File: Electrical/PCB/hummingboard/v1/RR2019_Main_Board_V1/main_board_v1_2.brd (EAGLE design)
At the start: 100 x 75 mm, 138 parts, among them CN1 MIRCO_B, IC1 OR_SC70-5, J10 I2C_5V_4, J11 SERVO_LEFT, J12 SERVO_RIGHT, J13 ESC, J14 5V_INPUT, J15 QUAD_ENCODER_2, J16 7.2V_INPUT, J17 I2C_5V_FXIO_1, J18 I2C_5V_FXIO_2, J19 JETSON_TRIGGER, J2 REAR_ENCODER, J20 QUAD_ENCODER_1, J21 BLDC_HALL, J22 SPI_FXIO_1, J3 FRONT_ENCODER, J4 I2C_3V3_1, J5 SPI_2, J6 WIRELESS_MODULE, J7 UART_0, J8 UART_2, J9 STEERING_ANGLE, Q1 BSS138, Q2 BSS138, Q3 DMP2066LSN, Q4 BSS138, Q5 BSS138, Q6 BSS138, Q7 BSS138, Q8 BSS138, U1 MPU-9250(IMU)

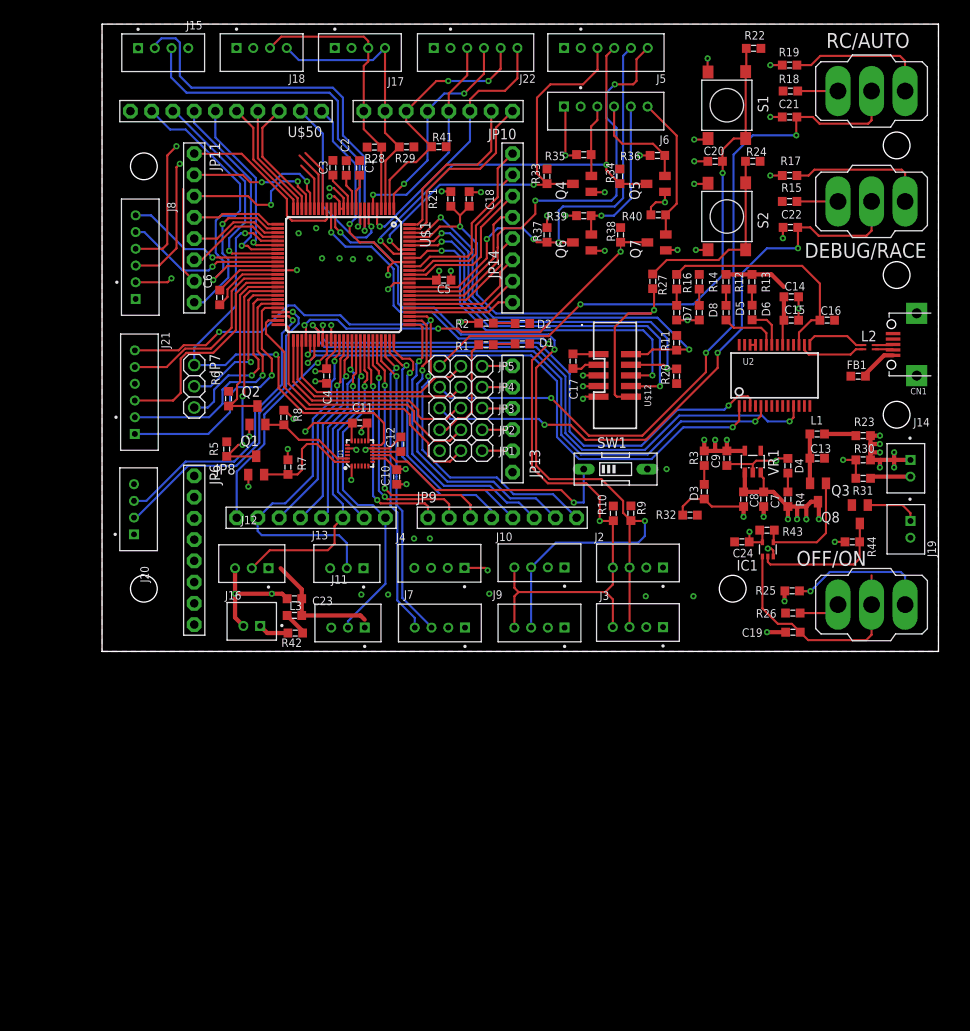
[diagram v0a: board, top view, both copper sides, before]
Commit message: add 1.8V LDO and IMU change to ICM-20948
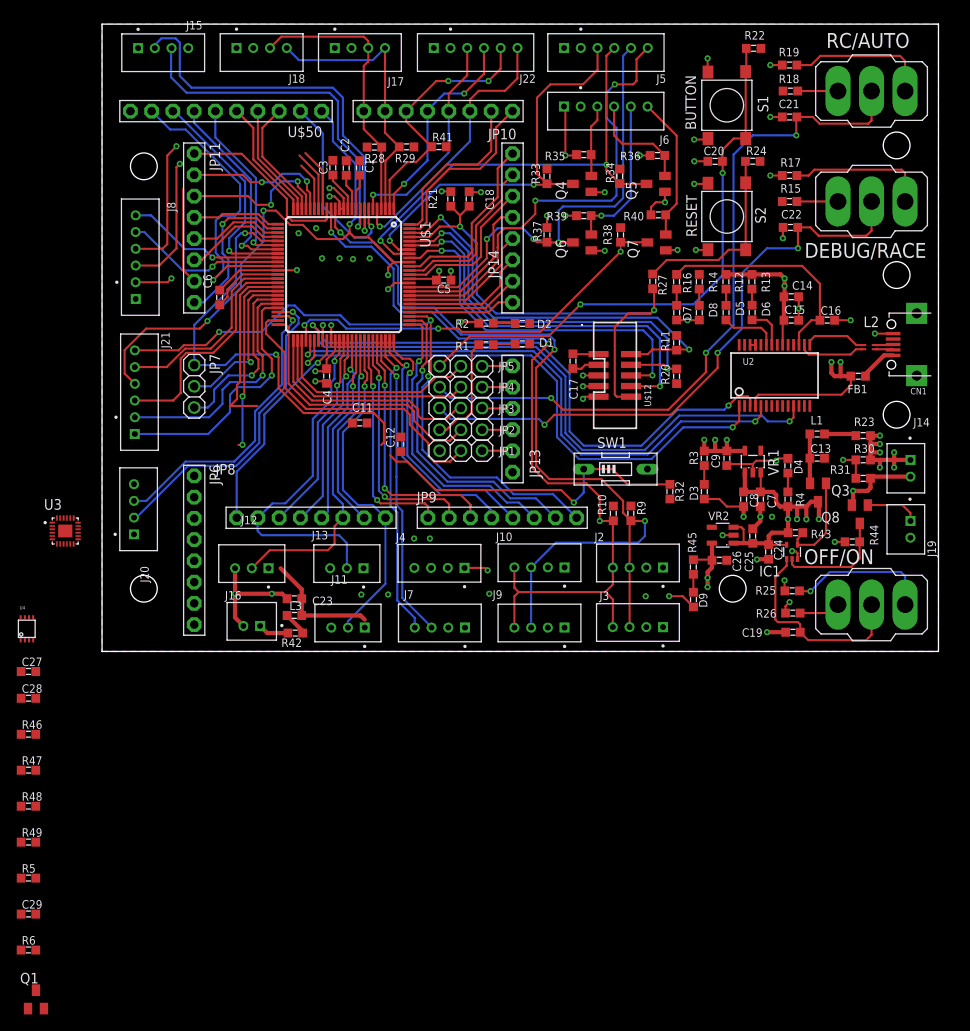
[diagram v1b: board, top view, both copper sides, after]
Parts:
- removed C10: 10nF, RobotRacing2019_Master:0603SMT
- removed Q2: BSS138, RobotRacing2019_Master:SOT23
- removed R7, R8: 10k, RobotRacing2019_Master:0603SMT
- removed U1: MPU-9250(IMU), RobotRacing2019_Master:QFN24-3X3
- added C25, C26: 1uF, RobotRacing2019_Master:0603SMT
- added C27, C28: 0.1u, RobotRacing2019_Master:0603SMT
- added C29: 0.1uF, RobotRacing2019_Master:0603SMT
- added D9: LED_GREEN, RobotRacing2019_Master:0603SMT
- added R45: 150, RobotRacing2019_Master:0603SMT
- added R46, R47, R48, R49: 1k, RobotRacing2019_Master:0603SMT
- added U3: ICM-20948, RobotRacing2019_Master:QFN40P300X300X105-25N
- added U4: PCA9306, RobotRacing2019_Master:PSOP-8
- added VR2: ADP121-AUJZ18, RobotRacing2019_Master:TSOT23-5
- D3, D4: value LED0603 -> LED_GREEN
- R3, R4: value (none) -> 150
- R5: value 10k -> 200k
- moved R6 70.1 mm to (-8.80, -35.7), turned to 0 degrees
- moved Q1 69.1 mm to (-7.90, -41.6)
- moved R5 56.5 mm to (-8.80, -27.1), turned to 0 degrees
- moved R32 3.69 mm to (67.9, 19.1), turned to 90 degrees
- moved C24 3.42 mm to (79.7, 11.9), turned to 90 degrees
- moved R43 3.41 mm to (82.9, 14.2)
- moved IC1 2.92 mm to (82.5, 11.9)
- moved C7 0.40 mm to (78.7, 18.2)
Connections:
- new net +1.8V: C11.2, C26.1, C27.2, C29.2, R45.2, R46.2, R47.2, R6.2, SW1.2, U3.13, U3.22, U3.8, U4.1, VR2.5
- new net I2C1_1.8_SCL: R46.1, U3.23, U4.2
- new net I2C_1.8_SDA: R47.1, U3.24, U4.3
- new net N$16: C28.2, R5.1, U4.7, U4.8
- new net N$37: Q1.1, U3.12
- new net N$42: D9.1, R45.1
- net +3V3: no longer C10.2, C11.2, Q1.1, Q2.1, R7.2, R8.2, SW1.2, U1.1, U1.13, U1.8
- net +VDD: now also C25.1, R48.2, R49.2, VR2.1, VR2.3; no longer R6.2
- net 3V3_SCL_1: no longer Q2.2, R8.1, U1.23
- net 3V3_SDA_1: no longer Q1.2, R7.1, U1.24
- net ADC0_SE10_/_ACMP0_IN5: now also Q1.3, R6.1; no longer U1.12
- net ADC0_SE14_/_PTC16: now also U3.11
- net GND: now also C25.2, C26.2, C27.1, C28.1, C29.1, D9.2, Q1.2, U3.18, U3.20, U3.25, U4.4, VR2.2; no longer C10.1, U1.11, U1.18, U1.20
- net I2C1_SDA: now also R49.1, U4.5; no longer Q1.3, R5.1
- net I2C1__SCL: now also R48.1, U4.6; no longer Q2.3, R6.1
- net N$10: now also U3.10; no longer U1.10
- net N$22: now also U3.9; no longer U1.9
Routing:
- net +1.8V: track 0.00 -> 129.0 mm, vias 0 -> 2
- net +VUSB: track 13.4 -> 64.7 mm, vias 0 -> 4
- net PTA11_/_FTM1_CH5: track 26.9 -> 70.8 mm, vias 2 -> 4
- net +3V3: track 45.9 -> 30.3 mm, vias 19 -> 11
- net 3V3_SDA_1: track 13.8 -> 0.00 mm
- net +VDD: track 65.3 -> 78.0 mm, vias 10 -> 11
- net 3V3_SCL_1: track 11.5 -> 0.00 mm
- net N$22: track 31.6 -> 39.9 mm
- net I2C1_SDA: track 28.1 -> 22.6 mm
- net POWER_SHUT_DOWN: track 28.2 -> 24.7 mm
- net N$10: track 3.40 -> 0.00 mm
- net N$39: track 14.3 -> 11.2 mm
- net N$38: track 16.2 -> 13.5 mm
- net N$31: track 88.4 -> 85.8 mm
- net N$42: track 0.00 -> 2.15 mm
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
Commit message: signal connection complete
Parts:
- moved Q1 75.6 mm to (22.2, 27.7)
- moved R6 72.1 mm to (19.2, 30.7), turned to 180 degrees
- moved C29 71.9 mm to (32.5, 27.4), turned to 180 degrees
- moved R47 56.7 mm to (33.9, 23.1), turned to 90 degrees
- moved R49 55.5 mm to (21.1, 23.9)
- moved R5 53.3 mm to (18.7, 18.5), turned to 180 degrees
- moved R48 48.2 mm to (18.7, 21.1), turned to 180 degrees
- moved R46 46.7 mm to (27.6, 19.3), turned to 270 degrees
- moved C27 40.6 mm to (25.5, 19.3), turned to 90 degrees
- moved C28 39.3 mm to (22.3, 18.5), turned to 180 degrees
- moved U4 36.5 mm to (22.5, 21.2), turned to 90 degrees
- moved U3 36.1 mm to (30.5, 23.8), turned to 180 degrees
- moved U$38 12.7 mm to (78.2, 3.20)
- moved C12 7.32 mm to (28.9, 27.5), turned to 180 degrees
- moved C11 5.10 mm to (27.0, 23.9), turned to 90 degrees
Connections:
- removed net 3V3_SCL_1: J4.3
- removed net 3V3_SDA_1: J4.4
- removed net I2C_1.8_SDA: R47.1, U3.24, U4.3
- new net I2C1_1.8_SDA: J4.4, R47.1, U3.24, U4.3
- net +1.8V: now also J4.1
- net +3V3: no longer J4.1
- net I2C1_1.8_SCL: now also J4.3
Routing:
- net ADC0_SE15_/_PTC17: track 23.0 -> 105.1 mm
- net I2C1_1.8_SDA: track 0.00 -> 27.5 mm, vias 0 -> 3
- net I2C1_1.8_SCL: track 0.00 -> 27.3 mm, vias 0 -> 1
- net GND: track 122.7 -> 148.1 mm, vias 42 -> 45
- net UART2_TX: track 23.3 -> 38.8 mm, vias 1 -> 2
- net ADC0_SE14_/_PTC16: track 21.6 -> 37.0 mm, vias 1 -> 2
- net FTM0_FLT0&2_/_TRGMUX_IN6_/_ACMP2_OUT: track 19.1 -> 33.0 mm, vias 0 -> 2
- net UART2_RX: track 22.0 -> 34.4 mm, vias 1 -> 2
- net ADC0_SE10_/_ACMP0_IN5: track 54.4 -> 42.3 mm
- net N$37: track 0.00 -> 9.80 mm
- net N$22: track 39.9 -> 49.5 mm
- net +1.8V: track 129.0 -> 137.9 mm, vias 2 -> 3
- net I2C1__SCL: track 21.9 -> 30.3 mm
- net N$16: track 0.00 -> 4.45 mm
- net I2C1_SDA: track 22.6 -> 26.8 mm, vias 2 -> 0
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- added copper zone on layer 1, net GND
- removed copper zone on layer 1, net +VDD

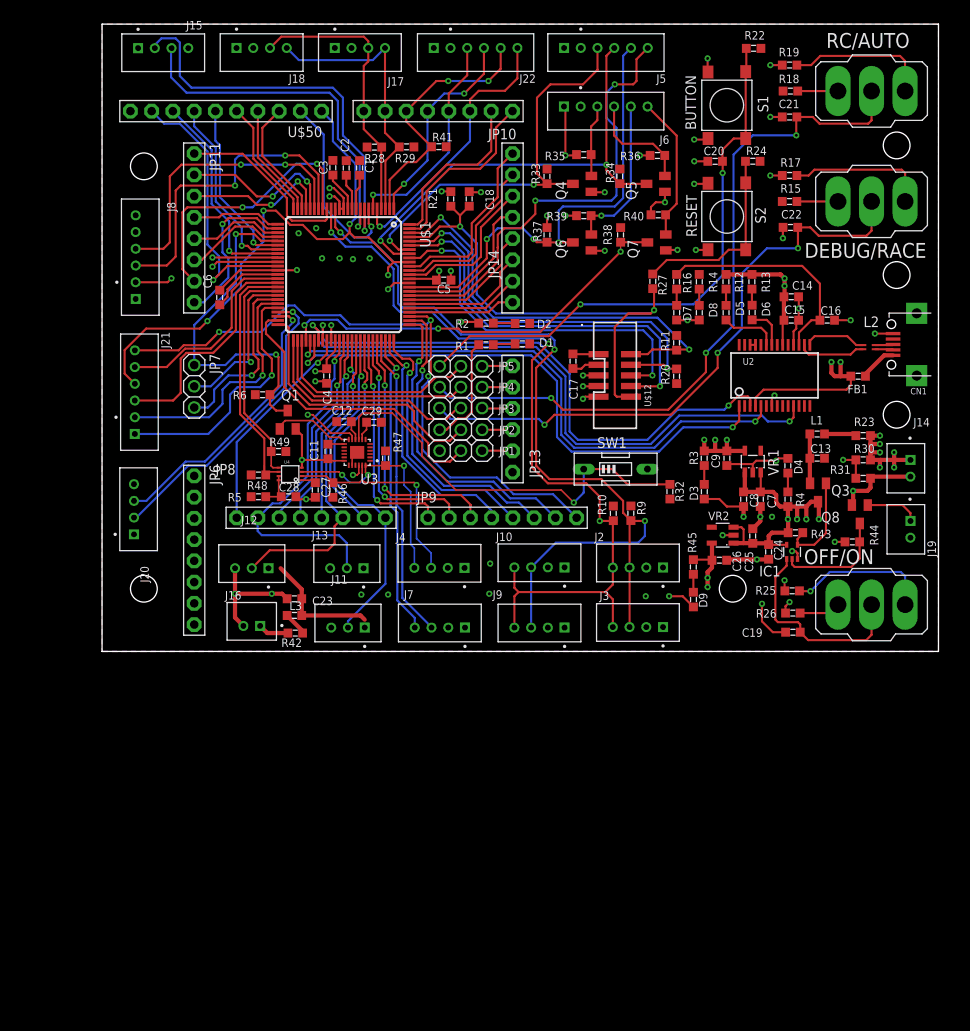
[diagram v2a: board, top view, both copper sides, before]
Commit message: add 1V8, 3V3, VUSB power plane
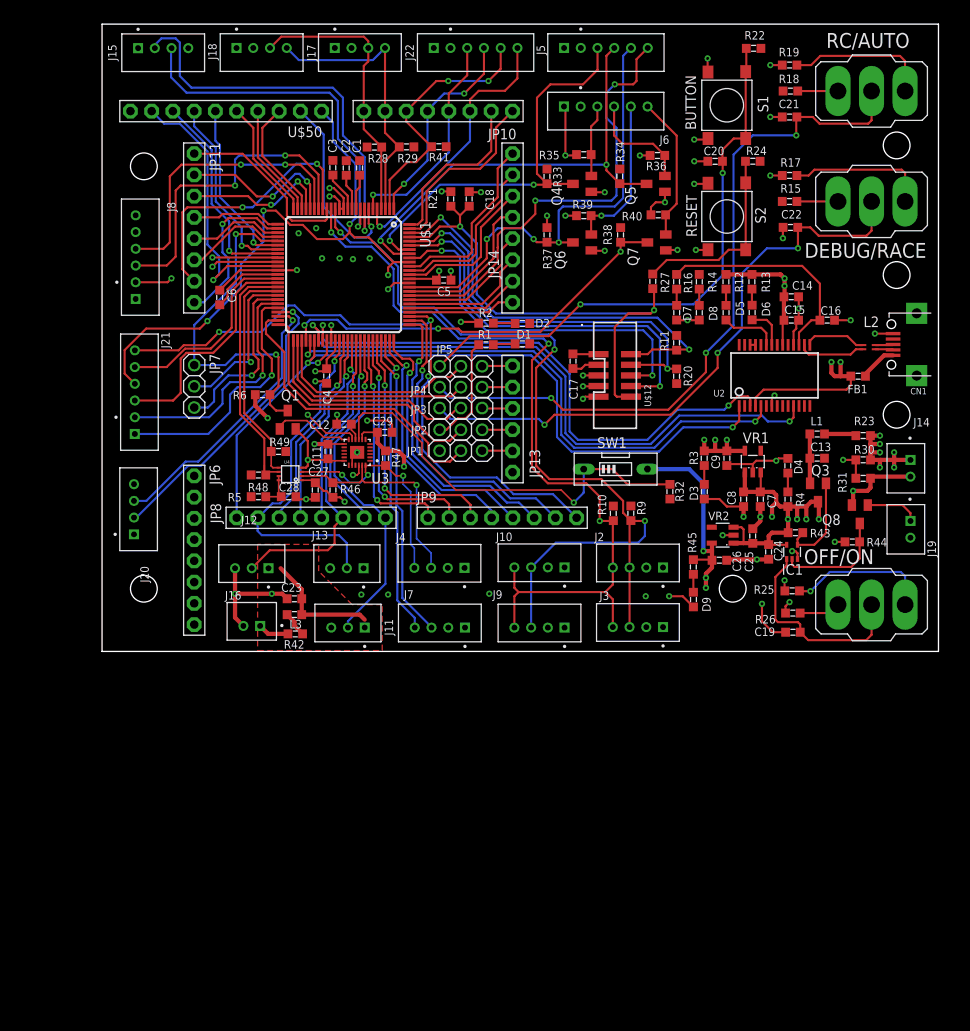
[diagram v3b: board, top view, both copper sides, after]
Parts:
- J4: value I2C_3V3_1 -> I2C_1V8_1
- moved C29 1.77 mm to (33.8, 26.2)
- moved C12 0.30 mm to (28.9, 27.2)
- moved L3 0.10 mm to (23.0, 4.40)
- moved R42 0.10 mm to (23.1, 2.10)
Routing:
- net +1.8V: track 137.9 -> 48.2 mm, vias 3 -> 8
- net GND: track 148.1 -> 153.6 mm, vias 45 -> 48
- net +VDD: track 78.0 -> 79.9 mm
- net I2C1_1.8_SDA: track 27.5 -> 26.7 mm
- net +3V3: vias 11 -> 10
- added copper zone on layer 15, net +1.8V
- added copper zone on layer 15, net +3V3
- added copper zone on layer 1, net +7.2V
- added copper zone on layer 15, net +VUSB
- removed copper zone on layer 1, net GND

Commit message: add silkscreen for pin info
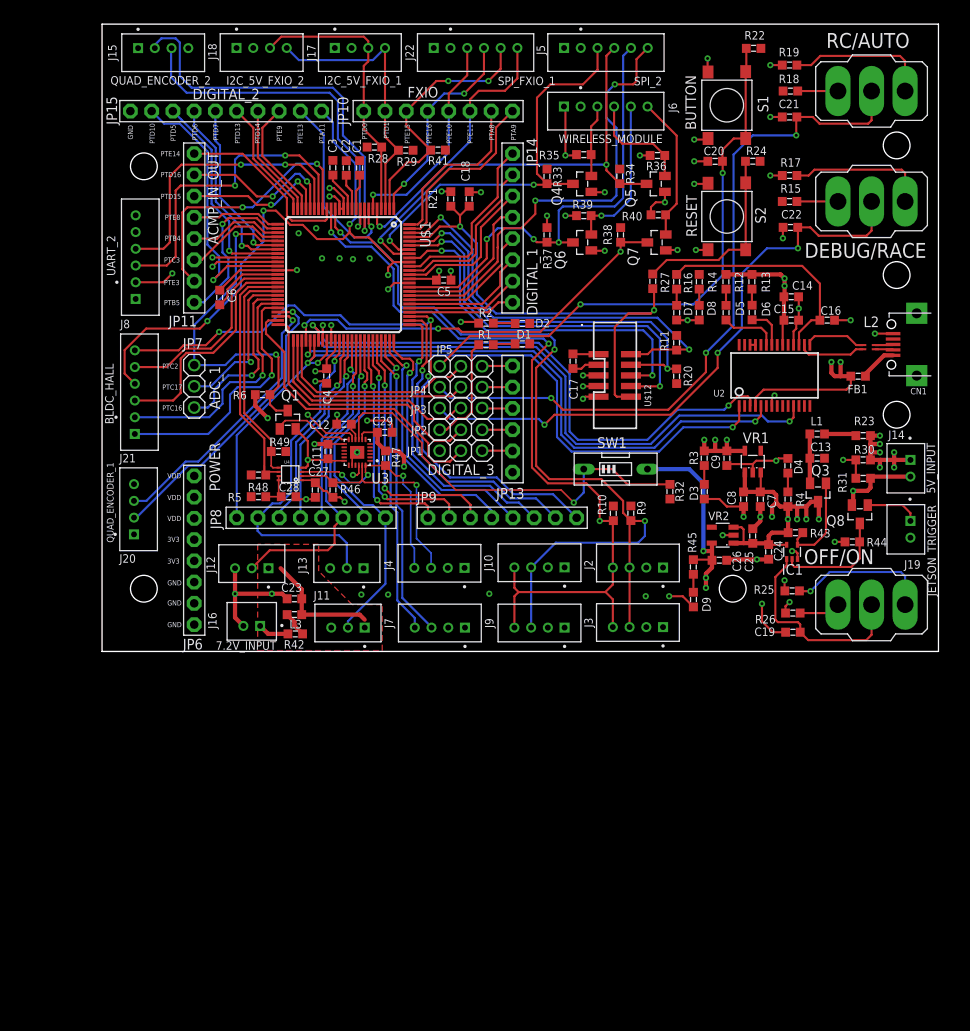
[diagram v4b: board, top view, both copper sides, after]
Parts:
- JP6: value POWER_1 -> POWER
- moved R41 0.41 mm to (40.2, 59.9)
- moved R29 0.41 mm to (36.3, 59.9)
- renumbered U$50 to JP15
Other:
- board text added: "3V3"
- board text added: "GND"
- board text added: "PTA11"
- board text added: "PTA8"
- board text added: "PTA9"
- board text added: "PTB4"
- board text added: "PTB5"
- board text added: "PTC16"
- board text added: "PTC17"
- board text added: "PTC2"
- board text added: "PTC3"
- board text added: "PTD0"
- board text added: "PTD1"
- board text added: "PTD10"
- board text added: "PTD13"
- board text added: "PTD14"
- board text added: "PTD15"
- board text added: "PTD16"
- board text added: "PTD5"
- board text added: "PTD6"
- board text added: "PTD7"
- board text added: "PTE10"
- board text added: "PTE11"
- board text added: "PTE13"
- board text added: "PTE14"
- board text added: "PTE15"
- board text added: "PTE16"
- board text added: "PTE3"
- board text added: "PTE8"
- board text added: "PTE9"
- board text added: "VDD"

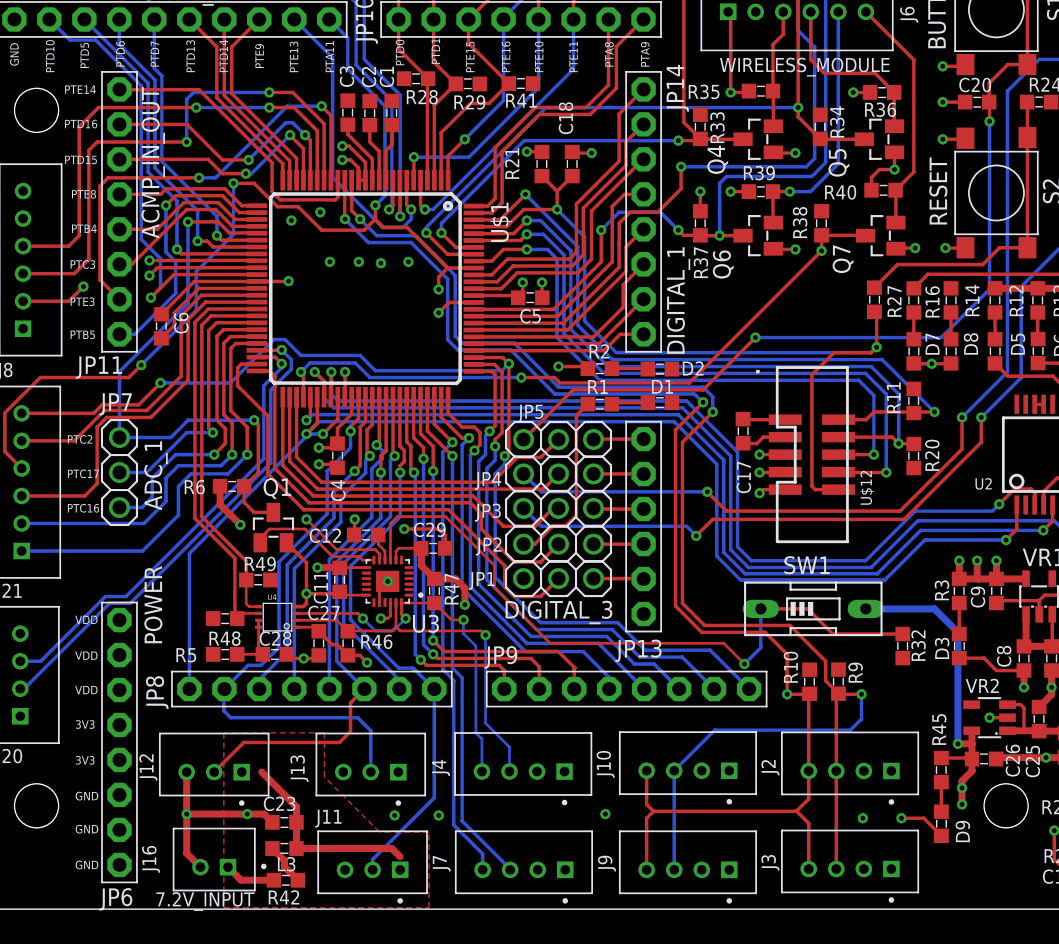
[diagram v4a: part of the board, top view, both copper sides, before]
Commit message: silkscreen complete for board
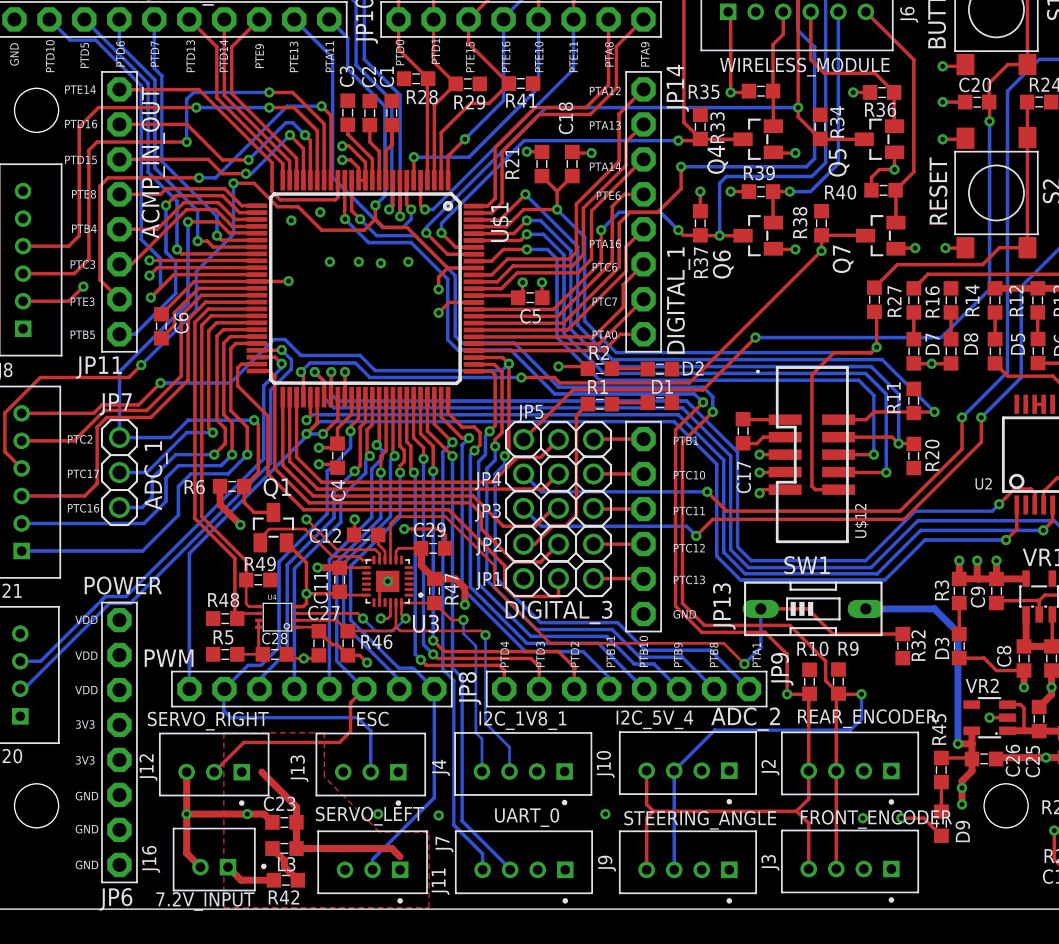
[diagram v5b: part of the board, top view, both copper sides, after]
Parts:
- U$12: value SWD_1.27MM -> SWD
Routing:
- net PTC13: track 36.3 -> 37.1 mm
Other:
- board text added: "PTA0"
- board text added: "PTA1"
- board text added: "PTA12"
- board text added: "PTA13"
- board text added: "PTA14"
- board text added: "PTA16"
- board text added: "PTB1"
- board text added: "PTB10"
- board text added: "PTB11"
- board text added: "PTB8"
- board text added: "PTB9"
- board text added: "PTC10"
- board text added: "PTC11"
- board text added: "PTC12"
- board text added: "PTC13"
- board text added: "PTC6"
- board text added: "PTC7"
- board text added: "PTD2"
- board text added: "PTD3"
- board text added: "PTD4"
- board text added: "PTE6"
